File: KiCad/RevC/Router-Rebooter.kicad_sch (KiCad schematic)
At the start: 18 parts, among them J1 12V Out, J2 ESP32 Power Bypass, J3 12V In, K1 OMRON G5LE-1-VD, Q1 PN2222A, U1 PSU2-5, U2 ESP32-C3-Zero

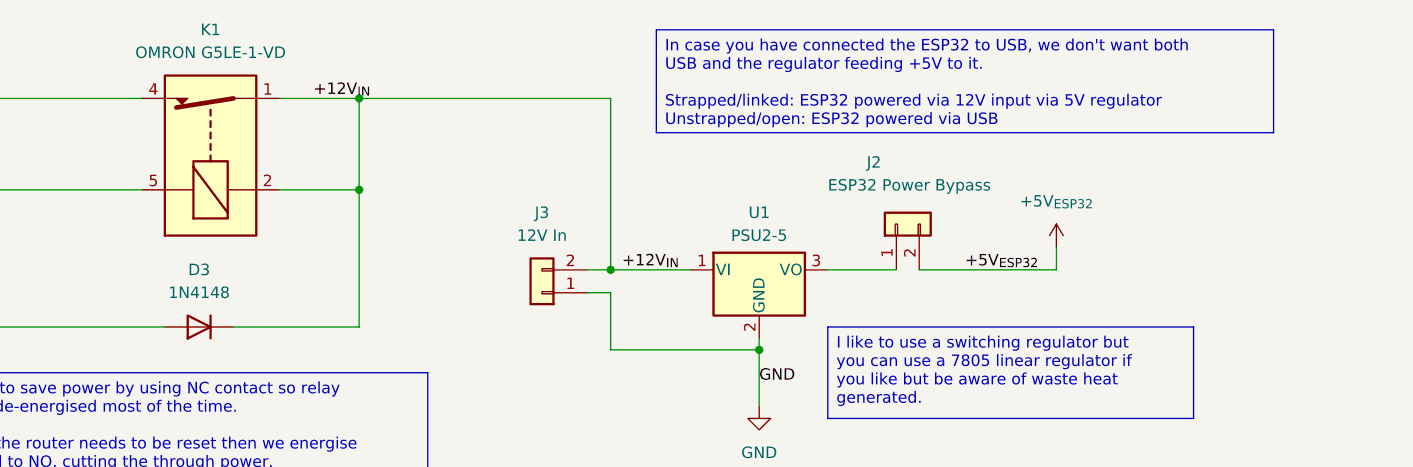
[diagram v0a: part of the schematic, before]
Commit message: Replaced D3, added D4
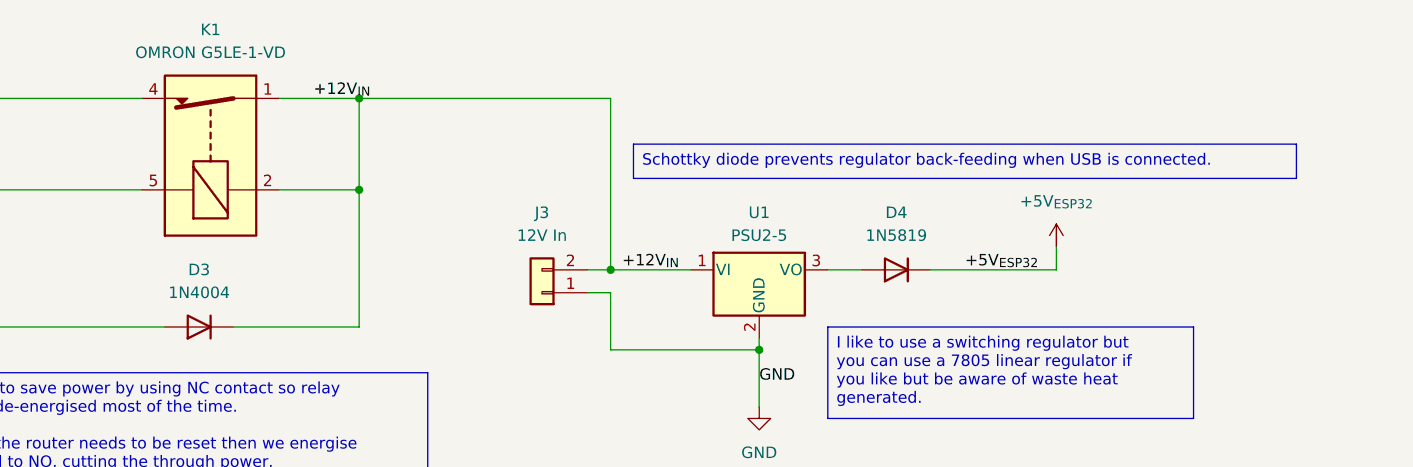
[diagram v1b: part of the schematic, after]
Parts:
- removed J2: ESP32 Power Bypass, Connector_PinHeader_2.54mm:PinHeader_1x02_P2.54mm_Vertical, symbol Connector_Generic:Conn_01x02
- added D4: 1N5819, Diode_THT:D_DO-41_SOD81_P10.16mm_Horizontal, symbol Device:D
- D3: value 1N4148 -> 1N4004; footprint Diode_THT:D_DO-35_SOD27_P7.62mm_Horizontal -> Diode_THT:D_DO-41_SOD81_P10.16mm_Horizontal
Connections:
- net +5V_{ESP32}: now also D4.1 (K)
- net at U1.3 (VO): now also D4.2 (A)
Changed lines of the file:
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@@
 		)
 	)
-	(text_box "In case you have connected the ESP32 to USB, we don't want both USB and the regulator feeding +5V to it.\n\nStrapped/linked: ESP32 powered via 12V input via 5V regulator\nUnstrapped/open: ESP32 powered via USB"
-		(exclude_from_sim no)
-		(at 195.58 50.8 0)
-		(size 68.58 11.43)
+	(text_box "Schottky diode prevents regulator back-feeding when USB is connected."
+		(exclude_from_sim no)
+		(at 193.04 63.5 0)
+		(size 73.66 3.81)
 		(margins 0.9525 0.9525 0.9525 0.9525)
 		(stroke
@@
 	(wire
 		(pts
-			(xy 224.79 77.47) (xy 240.03 77.47)
+			(xy 226.06 77.47) (xy 240.03 77.47)
 		)
 		(stroke
@@
 	(wire
 		(pts
+			(xy 218.44 77.47) (xy 214.63 77.47)
+		)
+		(stroke
+			(width 0)
+			(type default)
+		)
+	)
+	(wire
+		(pts
 			(xy 58.42 106.68) (xy 58.42 115.57)
 		)
@@
 		(pts
 			(xy 54.61 88.9) (xy 66.04 88.9)
-		)
-		(stroke
-			(width 0)
-			(type default)
-		)
-	)
-	(wire
-		(pts
-			(xy 214.63 77.47) (xy 222.25 77.47)
 		)
 		(stroke
@@
 				(path "/8de648ee-e13b-40be-adc8-7d40ce8ea697"
 					(reference "R1")
+					(unit 1)
+				)
+			)
+		)
+	)
+	(symbol
+		(lib_id "Device:D")
+		(at 222.25 77.47 180)
+		(unit 1)
+		(exclude_from_sim no)
+		(in_bom yes)
+		(on_board yes)
+		(dnp no)
+		(fields_autoplaced yes)
+		(property "Reference" "D4"
+			(at 222.25 71.12 0)
+			(effects
+				(font
+					(size 1.27 1.27)
+				)
+			)
+		)
+		(property "Value" "1N5819"
+			(at 222.25 73.66 0)
+			(effects
+				(font
+					(size 1.27 1.27)
+				)
+			)
+		)
+		(property "Footprint" "Diode_THT:D_DO-41_SOD81_P10.16mm_Horizontal"
+			(at 222.25 77.47 0)
+			(effects
+				(font
+					(size 1.27 1.27)
+				)
+				(hide yes)
+			)
+		)
+		(property "Datasheet" "~"
+			(at 222.25 77.47 0)
+			(effects
+				(font
+					(size 1.27 1.27)
+				)
+				(hide yes)
+			)
+		)
+		(property "Description" "Diode"
+			(at 222.25 77.47 0)
+			(effects
+				(font
+					(size 1.27 1.27)
+				)
+				(hide yes)
+			)
+		)
+		(property "Sim.Device" "D"
+			(at 222.25 77.47 0)
+			(effects
+				(font
+					(size 1.27 1.27)
+				)
+				(hide yes)
+			)
+		)
+		(property "Sim.Pins" "1=K 2=A"
+			(at 222.25 77.47 0)
+			(effects
+				(font
+					(size 1.27 1.27)
+				)
+				(hide yes)
+			)
+		)
+		(pin "1"
+		)
+		(pin "2"
+		)
+		(instances
+			(project "Router-Rebooter"
+				(path "/8de648ee-e13b-40be-adc8-7d40ce8ea697"
+					(reference "D4")
 					(unit 1)
 				)
@@
 			)
 		)
-		(property "Value" "1N4148"
+		(property "Value" "1N4004"
 			(at 144.78 80.01 0)
 			(effects
@@
 			)
 		)
-		(property "Footprint" "Diode_THT:D_DO-35_SOD27_P7.62mm_Horizontal"
+		(property "Footprint" "Diode_THT:D_DO-41_SOD81_P10.16mm_Horizontal"
 			(at 144.78 83.82 0)
 			(effects
@@
 					(unit 1)
 				)
-			)
-		)
-	)
-	(symbol
-		(lib_id "Connector_Generic:Conn_01x02")
-		(at 222.25 72.39 90)
-		(unit 1)
-		(exclude_from_sim no)
-		(in_bom yes)
-		(on_board yes)
-		(dnp no)
-		(property "Reference" "J2"
-			(at 218.948 65.532 90)
-			(effects
-				(font
-					(size 1.27 1.27)
-				)
-				(justify right)
-			)
-		)
-		(property "Value" "ESP32 Power Bypass"
-			(at 214.63 68.072 90)
-			(effects
-				(font
-					(size 1.27 1.27)
-				)
-				(justify right)
-			)
-		)
-		(property "Footprint" "Connector_PinHeader_2.54mm:PinHeader_1x02_P2.54mm_Vertical"
-			(at 222.25 72.39 0)
-			(effects
-				(font
-					(size 1.27 1.27)
-				)
-				(hide yes)
-			)
-		)
-		(property "Datasheet" "~"
-			(at 222.25 72.39 0)
-			(effects
-				(font
-					(size 1.27 1.27)
-				)
-				(hide yes)
-			)
-		)
-		(property "Description" "Generic connector, single row, 01x02, script generated (kicad-library-utils/schlib/autogen/connector/)"
-			(at 222.25 72.39 0)
-			(effects
-				(font
-					(size 1.27 1.27)
-				)
-				(hide yes)
-			)
-		)
-		(pin "2"
-		)
-		(pin "1"
-		)
-		(instances
-			(project ""
-				(path "/8de648ee-e13b-40be-adc8-7d40ce8ea697"
-					(reference "J2")
-					(unit 1)
-				)
